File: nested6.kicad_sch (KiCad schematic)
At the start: 20 parts, among them Q1 NMOS, U7 XL1509-5.0, U8 TP4056-42-ESOP8

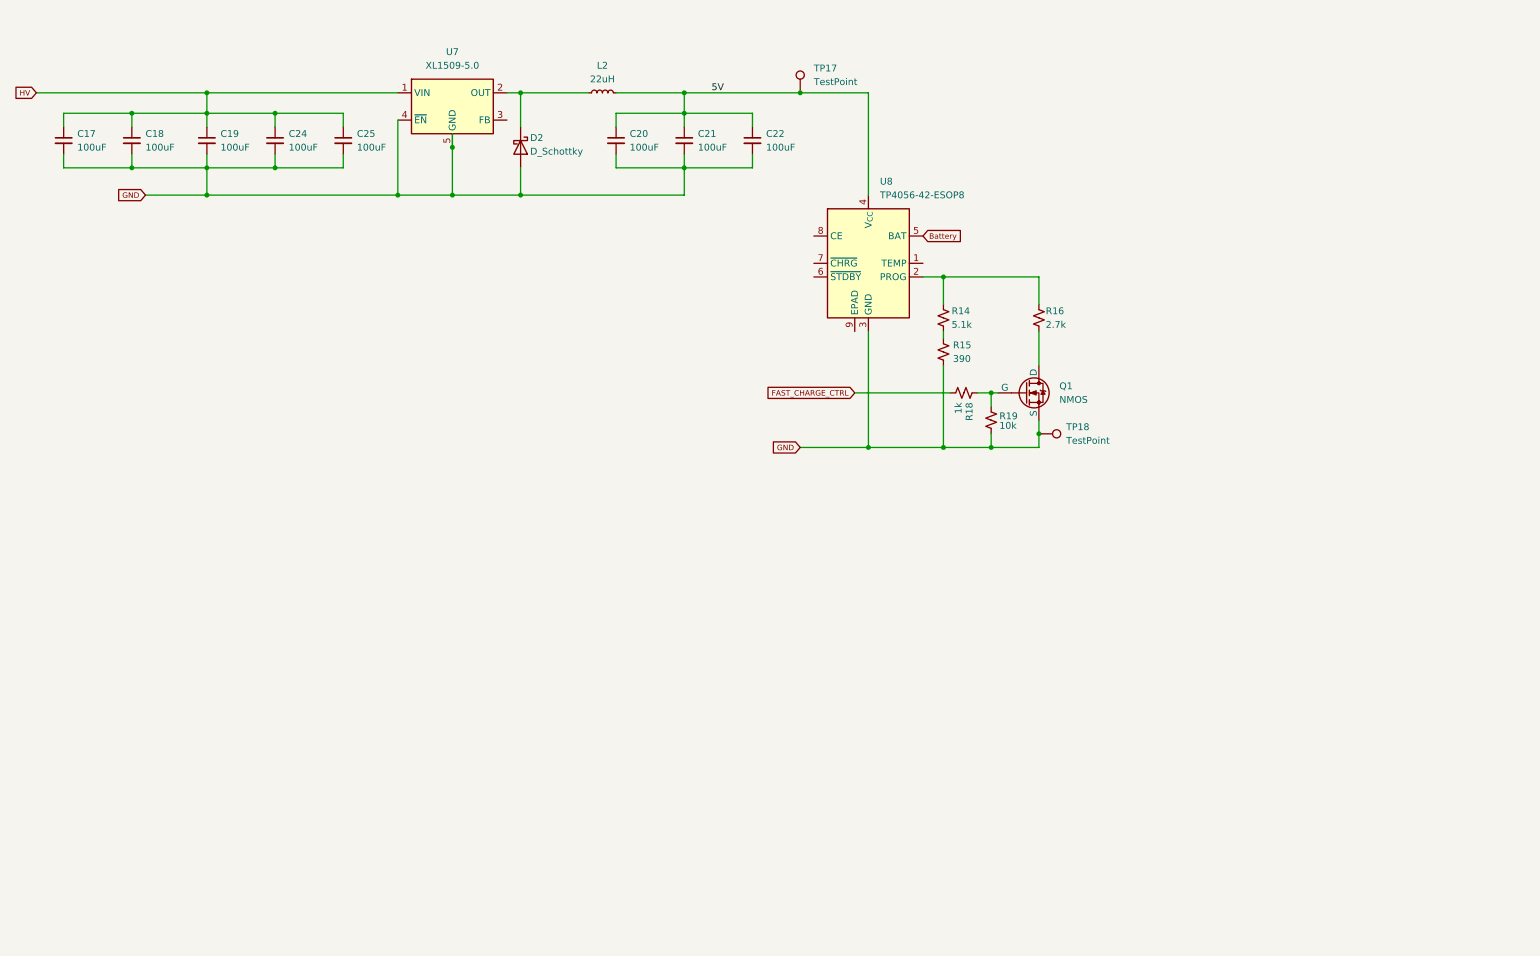
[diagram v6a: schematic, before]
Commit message: Removed old backups and updated KiCad files
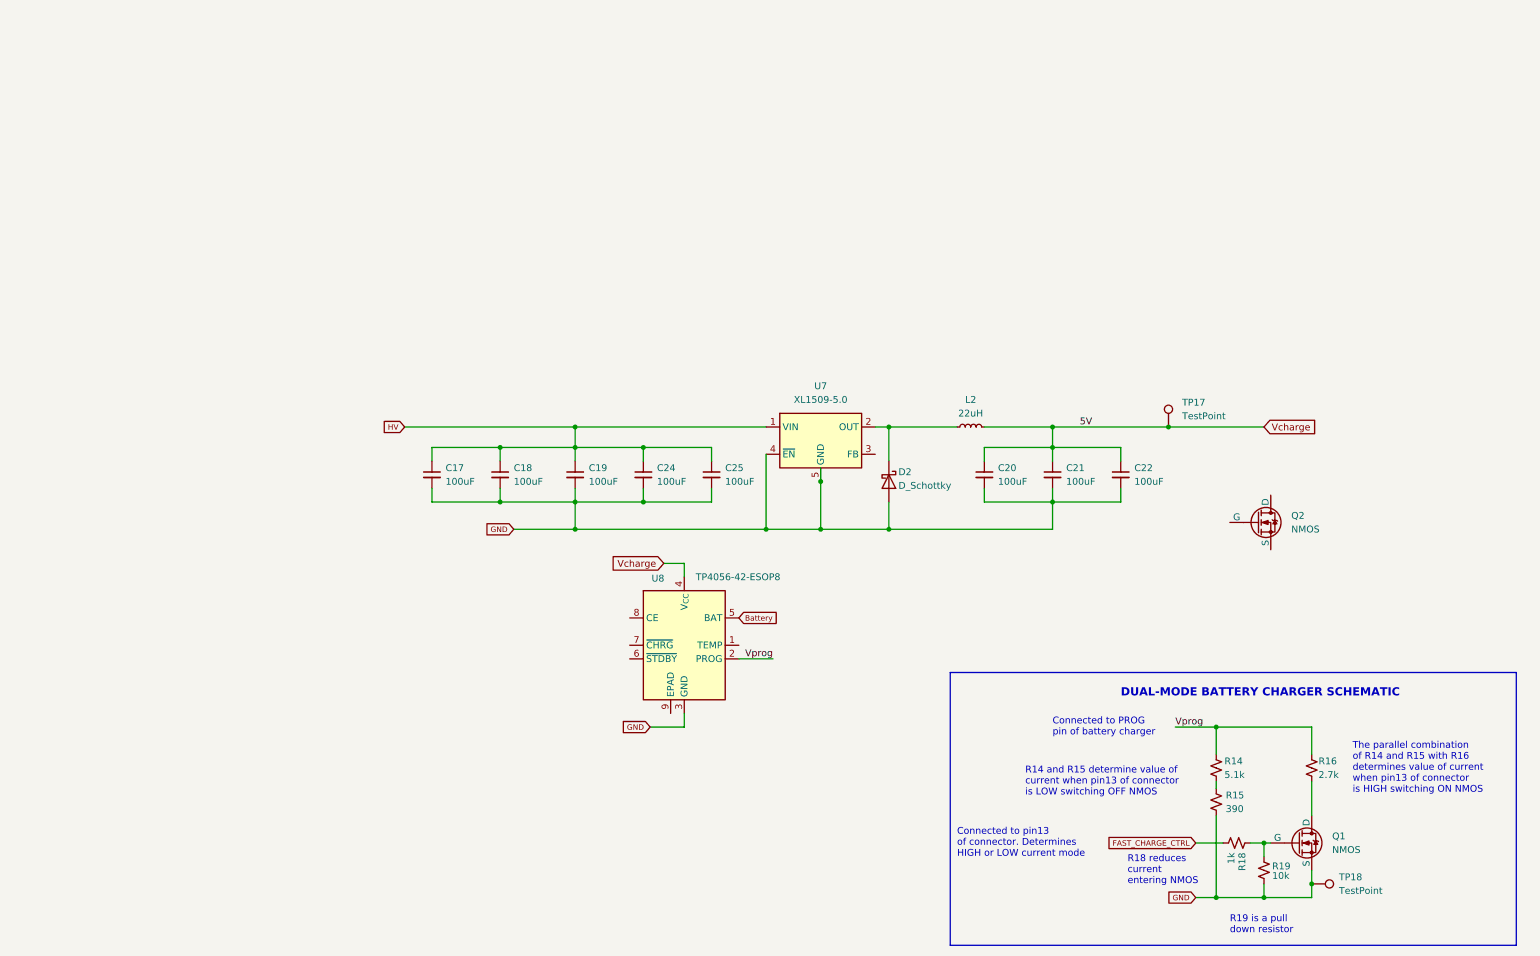
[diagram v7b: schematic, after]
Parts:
- added Q2: NMOS, Package_TO_SOT_SMD:SOT-23, symbol Simulation_SPICE:NMOS
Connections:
- net Vprog: now reaches R14.1, R16.1, U8.2 (PROG)
- net 5V renamed Vcharge
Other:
- note added: "Connected to PROG pin of battery charger"
- note added: "Connected to pin13 of connector. Determines HIGH or LOW current mode"
- note added: "DUAL-MODE BATTERY CHARGER SCHEMATIC"
- note added: "R14 and R15 determine value of current when pin13 of connector is LOW switching OFF NMOS"
- note added: "R18 reduces current entering NMOS"
- note added: "R19 is a pull down resistor"
- note added: "The parallel combination of R14 and R15 with R16 determines value of current when pin13 of connector is HIGH switching ON NMOS"
- company: (none) -> University of Cape Town
- title: (none) -> MICRO-MOUSE POWER SUBSYSTEM
- moved on the sheet: C17, C18, C19, C20, C21, C22, C24, C25, D2, L2, Q1, R14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
